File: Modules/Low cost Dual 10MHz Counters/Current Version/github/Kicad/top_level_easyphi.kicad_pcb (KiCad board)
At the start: 4 copper layers, 252 parts, among them J1 JTAG_CONNEC, J2 DM3D-SF(AS), P1 CONN_8, P2 CONN_20X2, Q1 MOS_P, Q2 FDD8780, Q3 FDD8780, U1 MAX5924D, U10 2-1825027-0, U11 RLP1-600-800, U12 TE-5650478-5, U13 SN74LVC1T45, U14 SN74LVC1G175, U15 TROU_FIX, U16 TROU_FIX, U17 RLP1-600-800, U18 RLP1-600-800, U19 RLP1-600-800, U2 MAX5925D, U20 RLP1-600-800, U21 RLP1-600-800, U22 CONNEC_QMA_ANO_2622-4035, U23 RLP1-600-800, U24 CONNEC_SMA_132203, U25 CONNEC_QMA_ANO_2622-4035, U26 CONNEC_SMA_132203, U27 CONNEC_SMA_132203, U28 CONNEC_QMA_ANO_2622-4035, U29 SY89840U, U3 24LC64, U30 NB4L52, U31 NB4L52, U32 MAX9203EKA-T, U33 SN74LVC1T45, U34 SN74LVC1T45, U35 TPS7A4901, U36 MAX9203EKA-T, U4 USBLC6-2, U5 TPS7A4901, U51 CARD_BORDER, U52 CARD_BORDER, U53 CARD_BORDER, U54 CARD_BORDER, U6 AOZ1280, U7 SAM3X8E, U8 SN74LVC2G240DCTR, U9 SN65LVDM176DGK, X1 12MHz, X2 32.768KHz

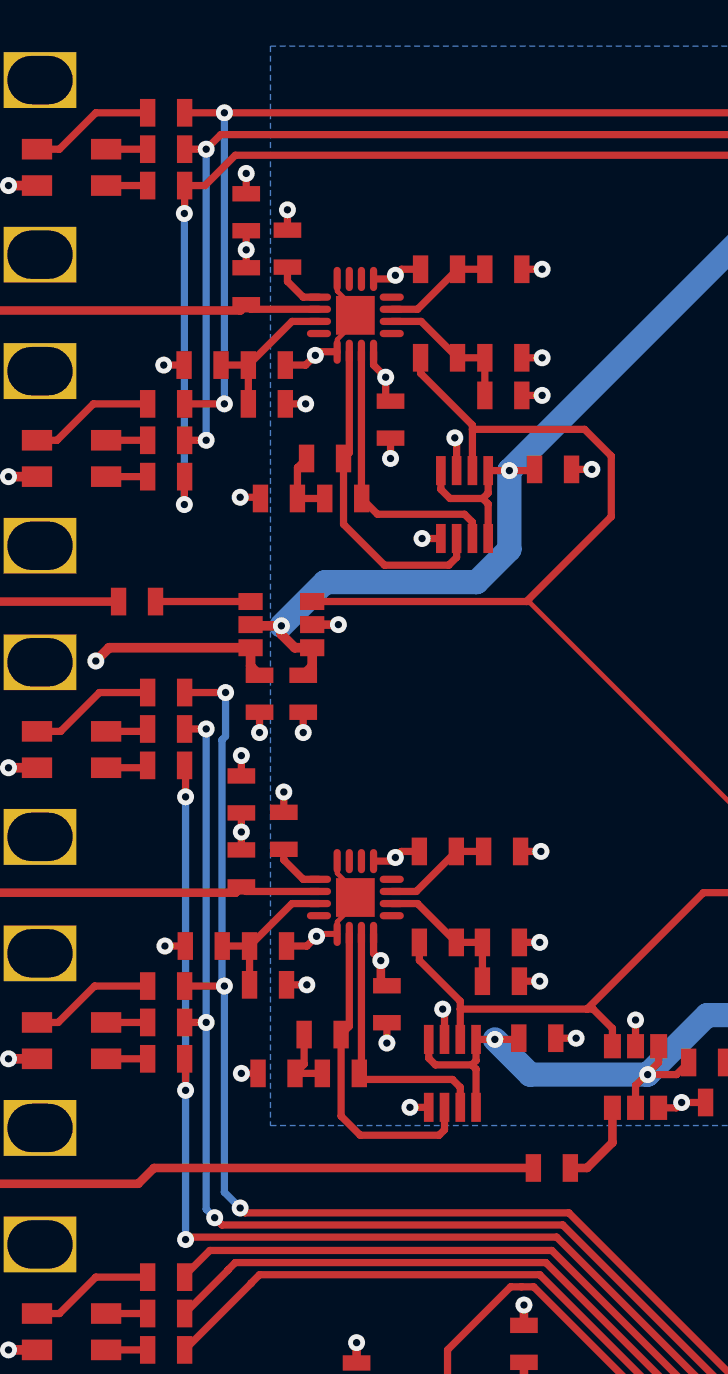
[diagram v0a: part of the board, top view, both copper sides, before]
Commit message: update counters
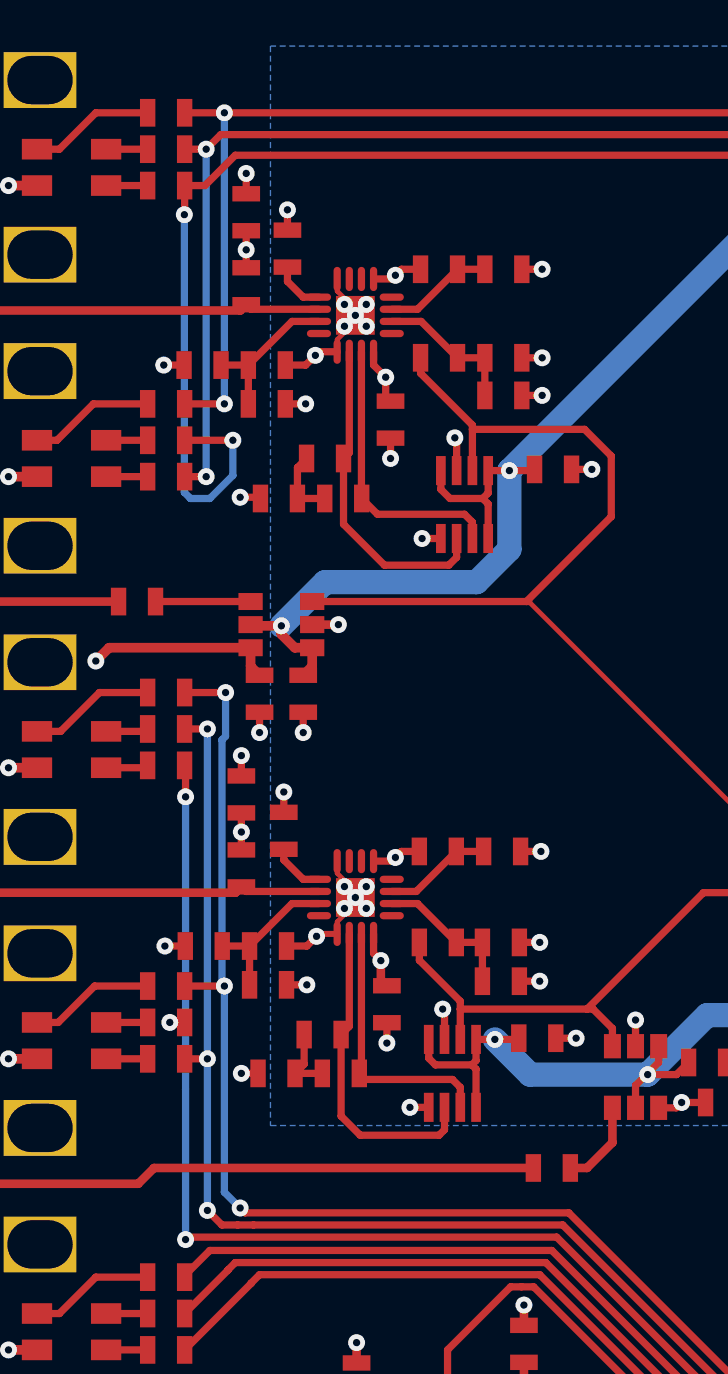
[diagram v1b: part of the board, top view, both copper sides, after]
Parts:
- C64, C65: value 1.5nF -> 22pF
- R93, R95: value 50 -> 1k
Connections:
- R46 pad 2: /template core easyphi/PWMH3/D7/PC9 -> /template core easyphi/PWMH2/D5/PC7
- R47 pad 2: /template core easyphi/PWMH2/D5/PC7 -> /template core easyphi/PWMH3/D7/PC9
- R50 pad 2: /template core easyphi/PWML6/A2/PC23 -> /template core easyphi/PWML5/A1/PC22
- R51 pad 2: /template core easyphi/PWML5/A1/PC22 -> /template core easyphi/PWML6/A2/PC23
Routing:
- net GND: track 583.1 -> 593.3 mm, vias 192 -> 202
- net /template core easyphi/PWMH3/D7/PC9: track 121.9 -> 126.2 mm
- net /template core easyphi/PWMH2/D5/PC7: track 122.0 -> 123.5 mm
